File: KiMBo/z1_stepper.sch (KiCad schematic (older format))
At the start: 23 parts, among them U21 TMC2130

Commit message: Assocate more footprints
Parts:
- C133, C134: footprint Capacitors_SMD:C_0402 -> Capacitors_SMD:C_0603
- R154, R155, R156, R157: footprint (none) -> Resistors_SMD:R_0603
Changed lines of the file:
@@
 F 0 "C134" H 9165 4146 50  0000 L CNN
 F 1 "22nF" H 9165 4055 50  0000 L CNN
-F 2 "Capacitors_SMD:C_0402" H 9088 3950 50  0001 C CNN
+F 2 "Capacitors_SMD:C_0603" H 9088 3950 50  0001 C CNN
 F 3 "" H 9050 4100 50  0000 C CNN
 	1    9050 4100
@@
 F 0 "R155" V 7100 3700 50  0000 C CNN
 F 1 "2.2Ω" V 7200 3700 50  0000 C CNN
-F 2 "" V 7130 3700 50  0001 C CNN
+F 2 "Resistors_SMD:R_0603" V 7130 3700 50  0001 C CNN
 F 3 "" H 7200 3700 50  0000 C CNN
 	1    7200 3700
@@
 F 0 "C133" H 7450 4000 50  0000 L CNN
 F 1 "4.7μF" H 7450 3800 50  0000 L CNN
-F 2 "Capacitors_SMD:C_0402" H 7438 3750 50  0001 C CNN
+F 2 "Capacitors_SMD:C_0603" H 7438 3750 50  0001 C CNN
 F 3 "" H 7400 3900 50  0000 C CNN
 	1    7400 3900
@@
 F 0 "R156" H 9219 6696 50  0000 L CNN
 F 1 "5.23kΩ" H 9219 6605 50  0000 L CNN
-F 2 "" V 9080 6650 50  0001 C CNN
+F 2 "Resistors_SMD:R_0603" V 9080 6650 50  0001 C CNN
 F 3 "" H 9150 6650 50  0000 C CNN
 	1    9150 6650
@@
 F 0 "R157" V 9150 6850 50  0000 C CNN
 F 1 "4.75kΩ" V 9250 6850 50  0000 C CNN
-F 2 "" V 9280 6850 50  0001 C CNN
+F 2 "Resistors_SMD:R_0603" V 9280 6850 50  0001 C CNN
 F 3 "" H 9350 6850 50  0000 C CNN
 	1    9350 6850
@@
 F 0 "R154" H 6369 4246 50  0000 L CNN
 F 1 "4.7kΩ" H 6369 4155 50  0000 L CNN
-F 2 "" V 6230 4200 50  0001 C CNN
+F 2 "Resistors_SMD:R_0603" V 6230 4200 50  0001 C CNN
 F 3 "" H 6300 4200 50  0000 C CNN
 	1    6300 4200

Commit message: More footprint association
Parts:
- R158, R159: footprint (none) -> Resistors_SMD:R_0805
- U21: footprint (none) -> KiMBo:QFN36_5X6
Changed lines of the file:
@@
 $EndComp
 $Comp
-L GND #PWR0218
+L GND #PWR0219
 U 1 1 58C0CFED
 P 7400 3250
-F 0 "#PWR0218" H 7400 3000 50  0001 C CNN
+F 0 "#PWR0219" H 7400 3000 50  0001 C CNN
 F 1 "GND" H 7400 3100 50  0000 C CNN
 F 2 "" H 7400 3250 50  0000 C CNN
@@
 $EndComp
 $Comp
-L GND #PWR0219
+L GND #PWR0220
 U 1 1 58C0CFFA
 P 10250 3300
-F 0 "#PWR0219" H 10250 3050 50  0001 C CNN
+F 0 "#PWR0220" H 10250 3050 50  0001 C CNN
 F 1 "GND" H 10255 3127 50  0000 C CNN
 F 2 "" H 10250 3300 50  0000 C CNN
@@
 $EndComp
 $Comp
-L +24V #PWR0220
+L +24V #PWR0221
 U 1 1 58C0D000
 P 8450 2800
-F 0 "#PWR0220" H 8450 2650 50  0001 C CNN
+F 0 "#PWR0221" H 8450 2650 50  0001 C CNN
 F 1 "+24V" H 8465 2973 50  0000 C CNN
 F 2 "" H 8450 2800 50  0000 C CNN
@@
 F 0 "R159" H 10600 6600 50  0000 R CNN
 F 1 "220mΩ" H 10600 6700 50  0000 R CNN
-F 2 "" V 10580 6650 50  0001 C CNN
+F 2 "Resistors_SMD:R_0805" V 10580 6650 50  0001 C CNN
 F 3 "" H 10650 6650 50  0000 C CNN
 	1    10650 6650
@@
 F 0 "R158" H 9800 6600 50  0000 R CNN
 F 1 "220mΩ" H 9800 6700 50  0000 R CNN
-F 2 "" V 9780 6650 50  0001 C CNN
+F 2 "Resistors_SMD:R_0805" V 9780 6650 50  0001 C CNN
 F 3 "" H 9850 6650 50  0000 C CNN
 	1    9850 6650
@@
 $EndComp
 $Comp
-L GND #PWR0221
+L GND #PWR0222
 U 1 1 58C0D01B
 P 9550 7000
-F 0 "#PWR0221" H 9550 6750 50  0001 C CNN
+F 0 "#PWR0222" H 9550 6750 50  0001 C CNN
 F 1 "GND" H 9555 6827 50  0000 C CNN
 F 2 "" H 9550 7000 50  0000 C CNN
@@
 NoConn ~ 7600 5650
 $Comp
-L GND #PWR0222
+L GND #PWR0223
 U 1 1 58C0D03E
 P 7550 6050
-F 0 "#PWR0222" H 7550 5800 50  0001 C CNN
+F 0 "#PWR0223" H 7550 5800 50  0001 C CNN
 F 1 "GND" H 7555 5877 50  0000 C CNN
 F 2 "" H 7550 6050 50  0000 C CNN
@@
 $EndComp
 $Comp
-L GND #PWR0223
+L GND #PWR0224
 U 1 1 58C0D082
 P 9150 5150
-F 0 "#PWR0223" H 9150 4900 50  0001 C CNN
+F 0 "#PWR0224" H 9150 4900 50  0001 C CNN
 F 1 "GND" H 9150 5000 50  0000 C CNN
 F 2 "" H 9150 5150 50  0000 C CNN
@@
 $EndComp
 $Comp
-L GND #PWR0224
+L GND #PWR0225
 U 1 1 58C0D096
 P 9150 6000
-F 0 "#PWR0224" H 9150 5750 50  0001 C CNN
+F 0 "#PWR0225" H 9150 5750 50  0001 C CNN
 F 1 "GND" H 9150 5850 50  0000 C CNN
 F 2 "" H 9150 6000 50  0000 C CNN
@@
 F 0 "U21" H 7850 6150 60  0000 C CNN
 F 1 "TMC2130" H 8600 6150 60  0000 C CNN
-F 2 "" H 8300 4950 60  0001 C CNN
+F 2 "KiMBo:QFN36_5X6" H 8300 4950 60  0001 C CNN
 F 3 "" H 8300 4950 60  0000 C CNN
 	1    8300 4650
@@
 	9000 4550 9300 4550
 $Comp
-L VDD_3V3B #PWR0225
+L VDD_3V3B #PWR0226
 U 1 1 5A314607
 P 6650 3400
-F 0 "#PWR0225" H 6650 3250 50  0001 C CNN
+F 0 "#PWR0226" H 6650 3250 50  0001 C CNN
 F 1 "VDD_3V3B" H 6665 3573 50  0000 C CNN
 F 2 "" H 6650 3400 50  0000 C CNN

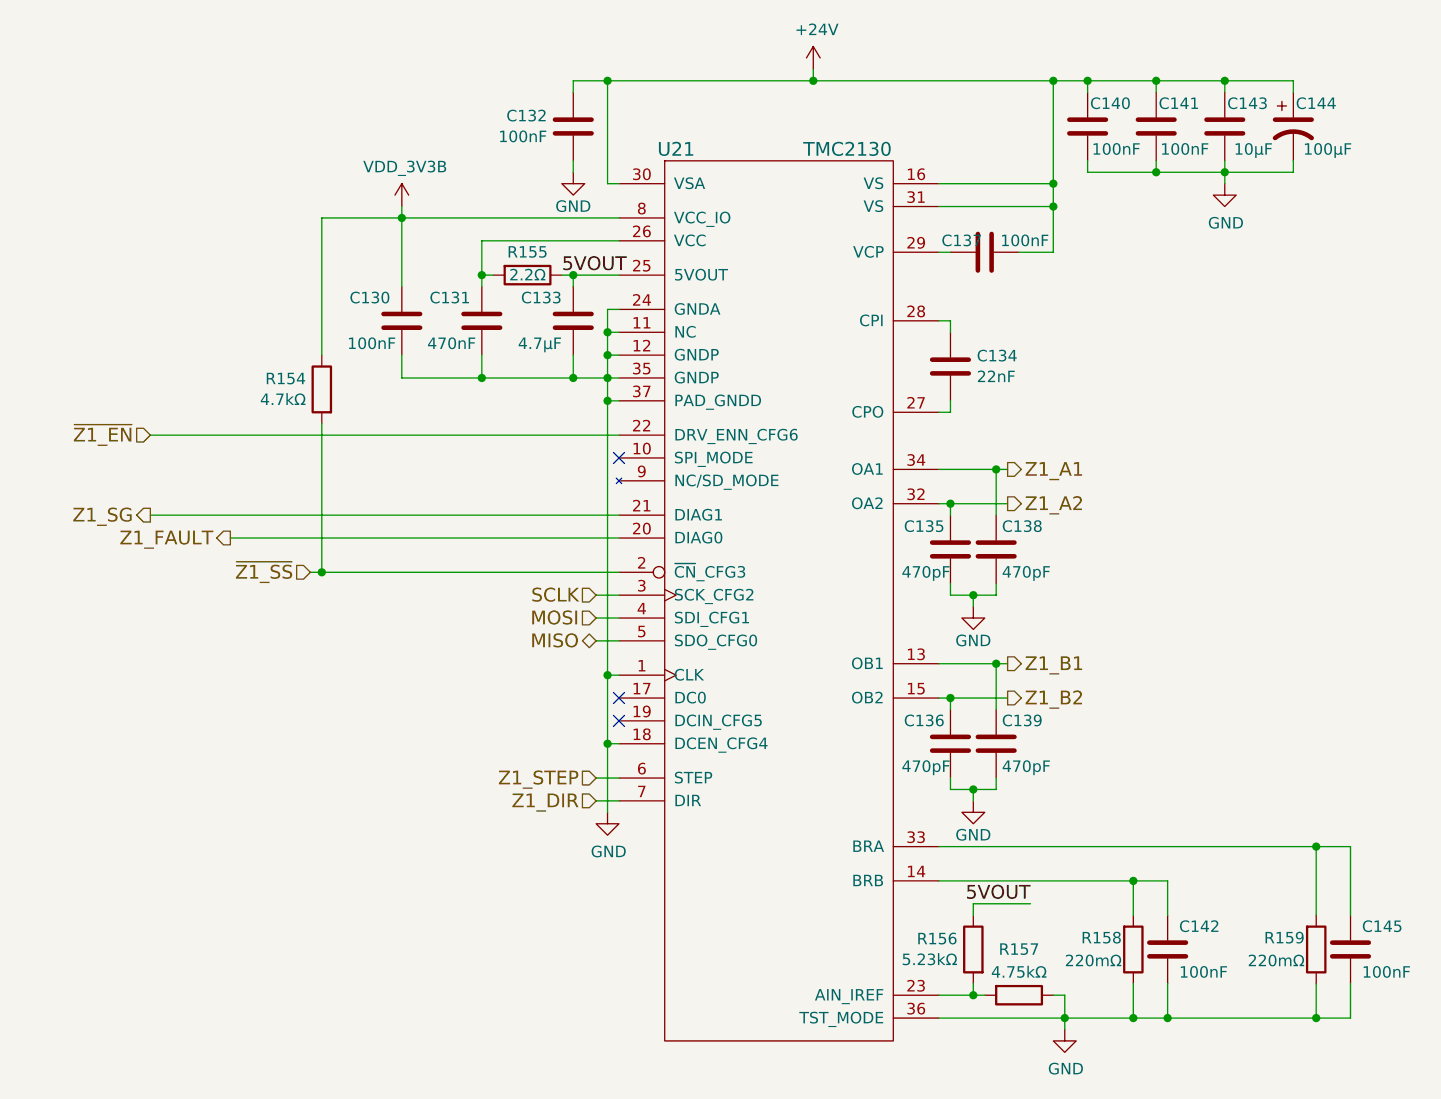
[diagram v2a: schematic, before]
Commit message: Add more footprints and more associations, one association left!
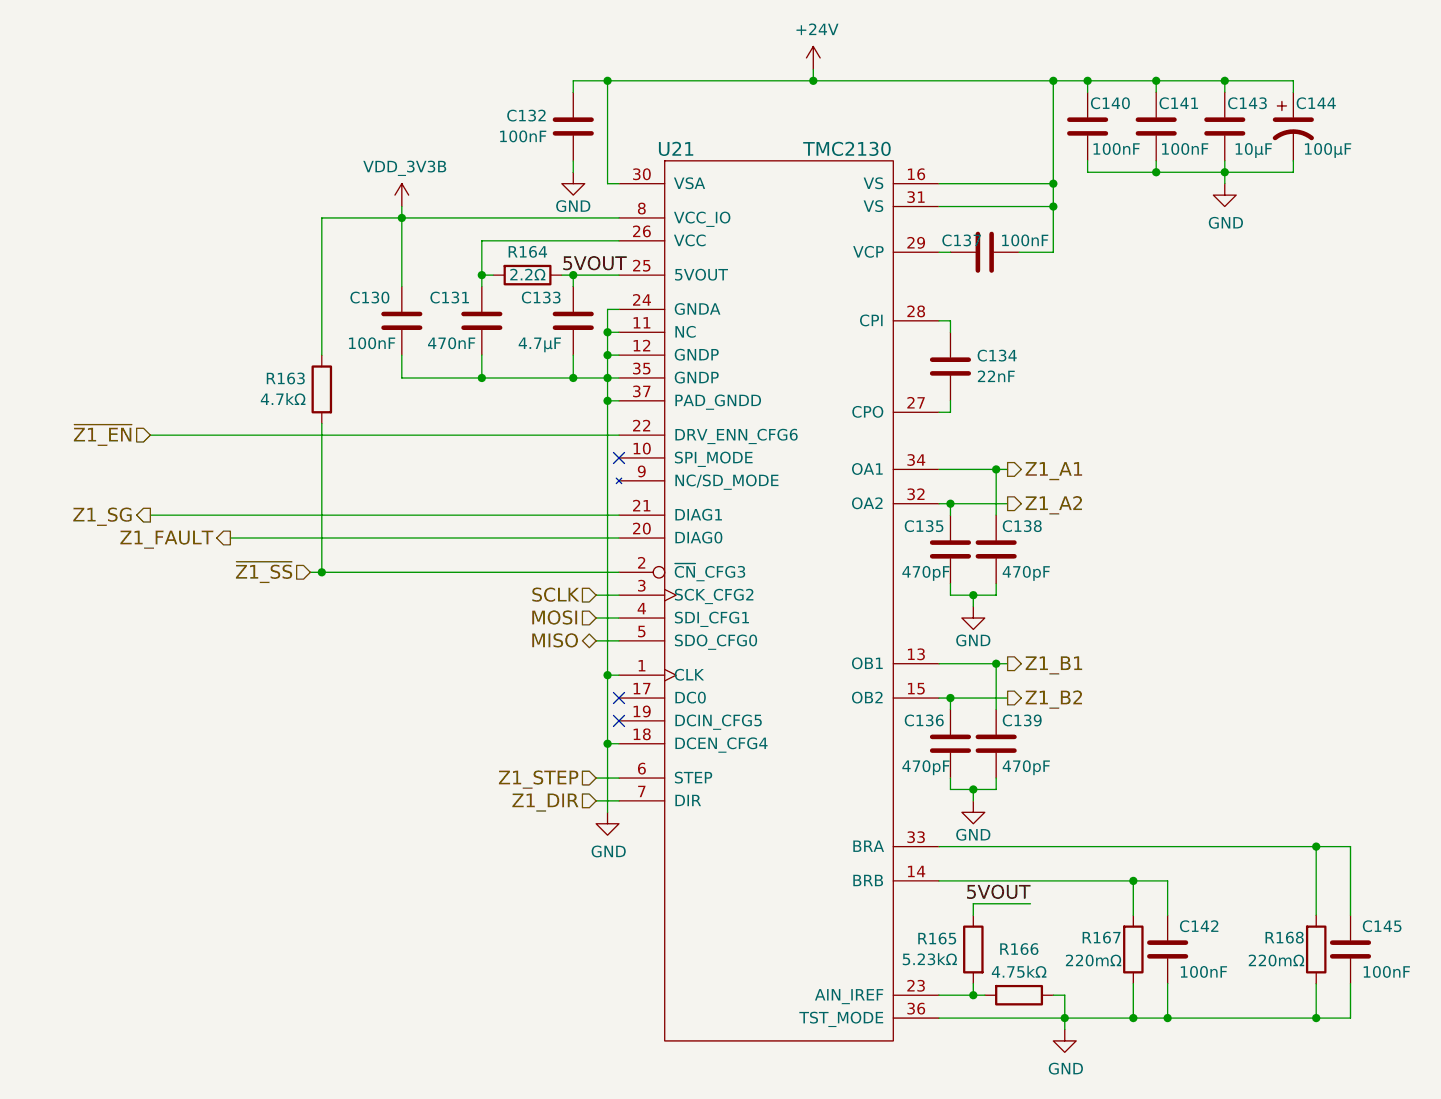
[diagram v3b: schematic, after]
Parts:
- R166: renamed from R157; footprint Resistors_SMD:R_0603 -> Resistors_SMD:R_0805
- R168: renamed from R159; footprint Resistors_SMD:R_0805 -> Resistors_SMD:R_0603
- renumbered R154 to R163, R155 to R164, R156 to R165, R158 to R167
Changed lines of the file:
@@
 $EndComp
 $Comp
-L GND #PWR0219
+L GND #PWR0221
 U 1 1 58C0CFED
 P 7400 3250
-F 0 "#PWR0219" H 7400 3000 50  0001 C CNN
+F 0 "#PWR0221" H 7400 3000 50  0001 C CNN
 F 1 "GND" H 7400 3100 50  0000 C CNN
 F 2 "" H 7400 3250 50  0000 C CNN
@@
 $EndComp
 $Comp
-L GND #PWR0220
+L GND #PWR0222
 U 1 1 58C0CFFA
 P 10250 3300
-F 0 "#PWR0220" H 10250 3050 50  0001 C CNN
+F 0 "#PWR0222" H 10250 3050 50  0001 C CNN
 F 1 "GND" H 10255 3127 50  0000 C CNN
 F 2 "" H 10250 3300 50  0000 C CNN
@@
 $EndComp
 $Comp
-L +24V #PWR0221
+L +24V #PWR0223
 U 1 1 58C0D000
 P 8450 2800
-F 0 "#PWR0221" H 8450 2650 50  0001 C CNN
+F 0 "#PWR0223" H 8450 2650 50  0001 C CNN
 F 1 "+24V" H 8465 2973 50  0000 C CNN
 F 2 "" H 8450 2800 50  0000 C CNN
@@
 $EndComp
 $Comp
-L R R159
+L R R168
 U 1 1 58C0D00D
 P 10650 6650
-F 0 "R159" H 10600 6600 50  0000 R CNN
+F 0 "R168" H 10600 6600 50  0000 R CNN
 F 1 "220mΩ" H 10600 6700 50  0000 R CNN
-F 2 "Resistors_SMD:R_0805" V 10580 6650 50  0001 C CNN
+F 2 "Resistors_SMD:R_0603" V 10580 6650 50  0001 C CNN
 F 3 "" H 10650 6650 50  0000 C CNN
 	1    10650 6650
@@
 $EndComp
 $Comp
-L R R158
+L R R167
 U 1 1 58C0D014
 P 9850 6650
-F 0 "R158" H 9800 6600 50  0000 R CNN
+F 0 "R167" H 9800 6600 50  0000 R CNN
 F 1 "220mΩ" H 9800 6700 50  0000 R CNN
 F 2 "Resistors_SMD:R_0805" V 9780 6650 50  0001 C CNN
@@
 $EndComp
 $Comp
-L GND #PWR0222
+L GND #PWR0224
 U 1 1 58C0D01B
 P 9550 7000
-F 0 "#PWR0222" H 9550 6750 50  0001 C CNN
+F 0 "#PWR0224" H 9550 6750 50  0001 C CNN
 F 1 "GND" H 9555 6827 50  0000 C CNN
 F 2 "" H 9550 7000 50  0000 C CNN
@@
 NoConn ~ 7600 5550
 $Comp
-L R R155
+L R R164
 U 1 1 58C0D022
 P 7200 3700
-F 0 "R155" V 7100 3700 50  0000 C CNN
+F 0 "R164" V 7100 3700 50  0000 C CNN
 F 1 "2.2Ω" V 7200 3700 50  0000 C CNN
 F 2 "Resistors_SMD:R_0603" V 7130 3700 50  0001 C CNN
@@
 NoConn ~ 7600 5650
 $Comp
-L GND #PWR0223
+L GND #PWR0225
 U 1 1 58C0D03E
 P 7550 6050
-F 0 "#PWR0223" H 7550 5800 50  0001 C CNN
+F 0 "#PWR0225" H 7550 5800 50  0001 C CNN
 F 1 "GND" H 7555 5877 50  0000 C CNN
 F 2 "" H 7550 6050 50  0000 C CNN
@@
 5VOUT
 $Comp
-L R R156
+L R R165
 U 1 1 58C0D05E
 P 9150 6650
-F 0 "R156" H 9219 6696 50  0000 L CNN
+F 0 "R165" H 9219 6696 50  0000 L CNN
 F 1 "5.23kΩ" H 9219 6605 50  0000 L CNN
 F 2 "Resistors_SMD:R_0603" V 9080 6650 50  0001 C CNN
@@
 5VOUT
 $Comp
-L R R157
+L R R166
 U 1 1 58C0D066
 P 9350 6850
-F 0 "R157" V 9150 6850 50  0000 C CNN
+F 0 "R166" V 9150 6850 50  0000 C CNN
 F 1 "4.75kΩ" V 9250 6850 50  0000 C CNN
-F 2 "Resistors_SMD:R_0603" V 9280 6850 50  0001 C CNN
+F 2 "Resistors_SMD:R_0805" V 9280 6850 50  0001 C CNN
 F 3 "" H 9350 6850 50  0000 C CNN
 	1    9350 6850
@@
 $EndComp
 $Comp
-L R R154
+L R R163
 U 1 1 58C0D06D
 P 6300 4200
-F 0 "R154" H 6369 4246 50  0000 L CNN
+F 0 "R163" H 6369 4246 50  0000 L CNN
 F 1 "4.7kΩ" H 6369 4155 50  0000 L CNN
 F 2 "Resistors_SMD:R_0603" V 6230 4200 50  0001 C CNN
@@
 $EndComp
 $Comp
-L GND #PWR0224
+L GND #PWR0226
 U 1 1 58C0D082
 P 9150 5150
-F 0 "#PWR0224" H 9150 4900 50  0001 C CNN
+F 0 "#PWR0226" H 9150 4900 50  0001 C CNN
 F 1 "GND" H 9150 5000 50  0000 C CNN
 F 2 "" H 9150 5150 50  0000 C CNN
@@
 $EndComp
 $Comp
-L GND #PWR0225
+L GND #PWR0227
 U 1 1 58C0D096
 P 9150 6000
-F 0 "#PWR0225" H 9150 5750 50  0001 C CNN
+F 0 "#PWR0227" H 9150 5750 50  0001 C CNN
 F 1 "GND" H 9150 5850 50  0000 C CNN
 F 2 "" H 9150 6000 50  0000 C CNN
@@
 	9000 4550 9300 4550
 $Comp
-L VDD_3V3B #PWR0226
+L VDD_3V3B #PWR0228
 U 1 1 5A314607
 P 6650 3400
-F 0 "#PWR0226" H 6650 3250 50  0001 C CNN
+F 0 "#PWR0228" H 6650 3250 50  0001 C CNN
 F 1 "VDD_3V3B" H 6665 3573 50  0000 C CNN
 F 2 "" H 6650 3400 50  0000 C CNN
